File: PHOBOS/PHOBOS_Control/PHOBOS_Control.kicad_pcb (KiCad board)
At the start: 2 copper layers, 34.7 x 49.9 mm, 76 parts, among them J2 Conn_Coaxial, J3 USB4056-03-A_REVA2, J4 Screw_Terminal_01x02, J7 Conn_01x05, J8 Conn_01x02, U1 SX1280IMLTRT, U2 W25Q128JVSIQ, U3 NCP1117-3.3_SOT223, U4 RP2040, U5 TLV9351IDCKR, U6 TLV9351IDCKR, U7 TLV9351IDCKR, U8 TLV9351IDCKR, Y1 C1E-52.000-10-1012-X-M, Y2 ABM8-272-T3

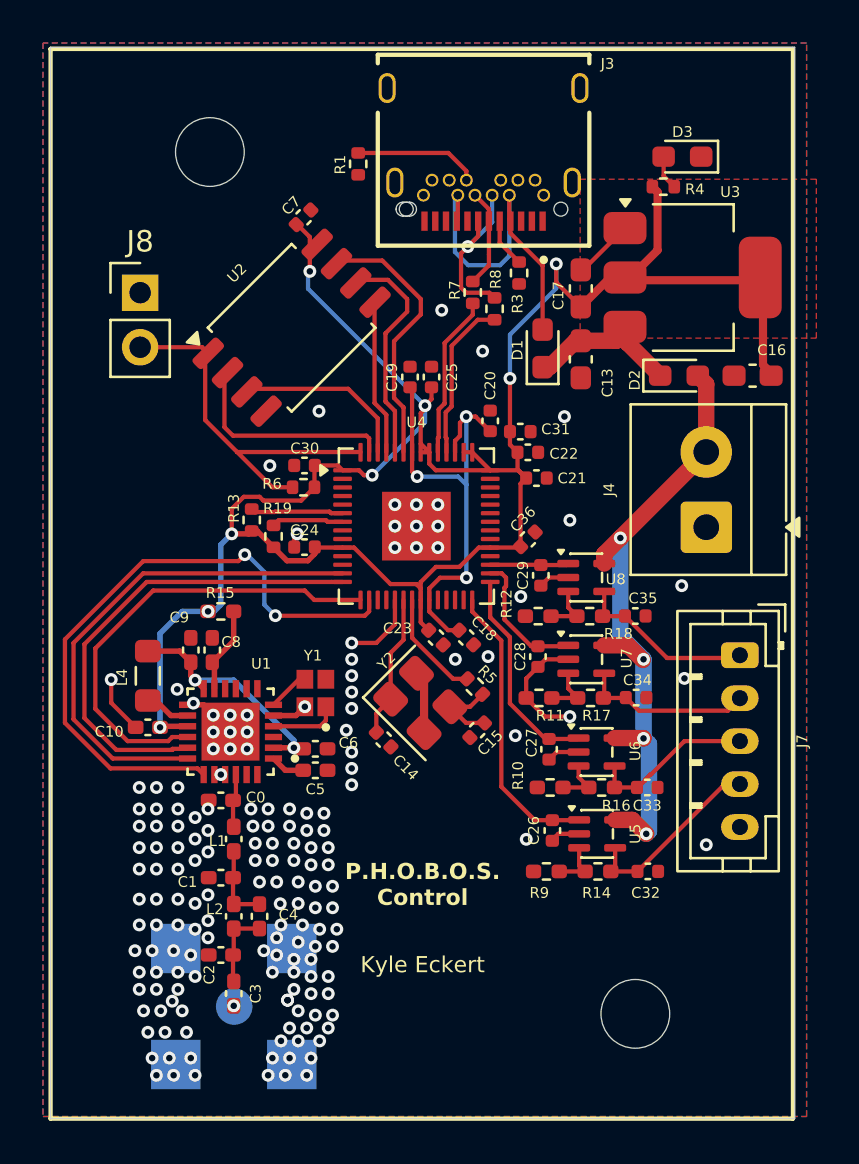
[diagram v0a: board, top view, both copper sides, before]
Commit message: drc updated. 33 usb error. silkscreen warnings
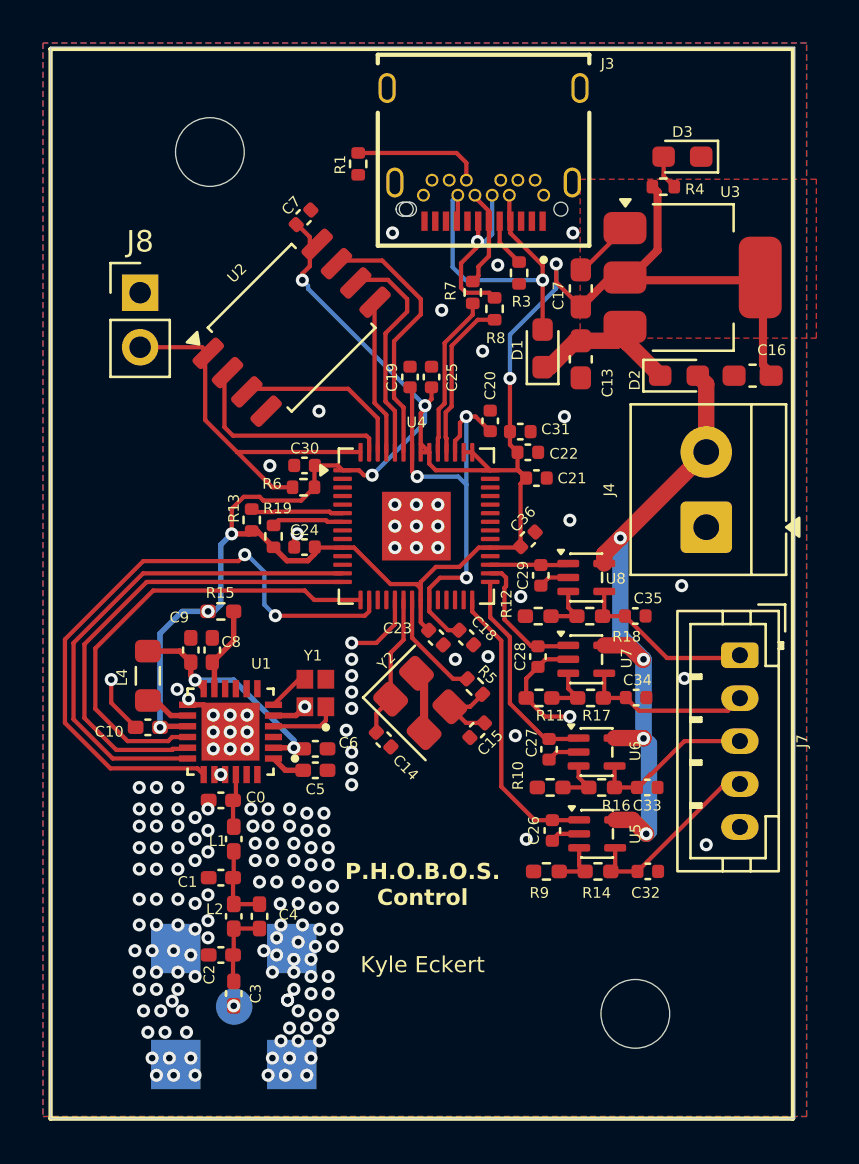
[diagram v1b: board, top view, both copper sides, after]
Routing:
- net VBUS: track 16.6 -> 16.0 mm, vias 0 -> 1
- net GND: vias 169 -> 172
